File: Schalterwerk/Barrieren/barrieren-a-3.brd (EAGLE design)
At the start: 71.1 x 80 mm, 75 parts, among them Q1 BSS84, Q2 BSS84, Q3 BSS84, Q4 BSS84, Q5 BSS84, Q6 BSS84, X1 PHNX_4P_350CONN_1984989_PXC, X2 PHNX_4P_350CONN_1984989_PXC, X3 PHNX_4P_350CONN_1984989_PXC, X4 PHNX_4P_350CONN_1984989_PXC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

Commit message: Routes the airwires
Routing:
- net GND: track 0.00 -> 173.8 mm, vias 0 -> 6
- net +24V: track 0.00 -> 129.2 mm, vias 0 -> 4
- net +15V: track 0.00 -> 77.0 mm
- net AGND: track 0.00 -> 69.8 mm
- net N$13: track 0.00 -> 51.4 mm
- net +12V: track 0.00 -> 48.5 mm, vias 0 -> 5
- net B3-IS-OP-SCH: track 0.00 -> 43.6 mm, vias 0 -> 1
- net B2-IS-OP-SCH: track 0.00 -> 43.2 mm, vias 0 -> 1
- net B3-IS-CL-SCH: track 0.00 -> 42.2 mm, vias 0 -> 1
- net B2-IS-CL-SCH: track 0.00 -> 42.0 mm, vias 0 -> 1
- net N$20: track 0.00 -> 38.4 mm
- net B3-ACT-CL: track 0.00 -> 36.3 mm
- net N$34: track 0.00 -> 34.7 mm
- net N$31: track 0.00 -> 34.2 mm
- net B2-IS-OP: track 0.00 -> 33.5 mm
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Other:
- board text added: "12V"
- board text added: "24V"

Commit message: removes unneeded mounting hole.
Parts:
- removed H1: MOUNT-HOLE3.3, holes:3,3
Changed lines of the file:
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@@
 <attribute name="NAME" x="57.15" y="30.48" size="1.27" layer="25" font="vector" ratio="10" rot="R180"/>
-</element>
-<element name="H1" library="holes" library_urn="urn:adsk.eagle:library:237" package="3,3" package3d_urn="urn:adsk.eagle:package:14278/1" value="MOUNT-HOLE3.3" x="31.623" y="88.9" smashed="yes" rot="MR0">
-<attribute name="POPULARITY" value="3" x="31.623" y="88.9" size="1.27" layer="28" font="vector" rot="MR0" display="off"/>
 </element>
 <element name="H2" library="holes" library_urn="urn:adsk.eagle:library:237" package="3,3" package3d_urn="urn:adsk.eagle:package:14278/1" value="MOUNT-HOLE3.3" x="4.953" y="5.08" smashed="yes" rot="MR0">

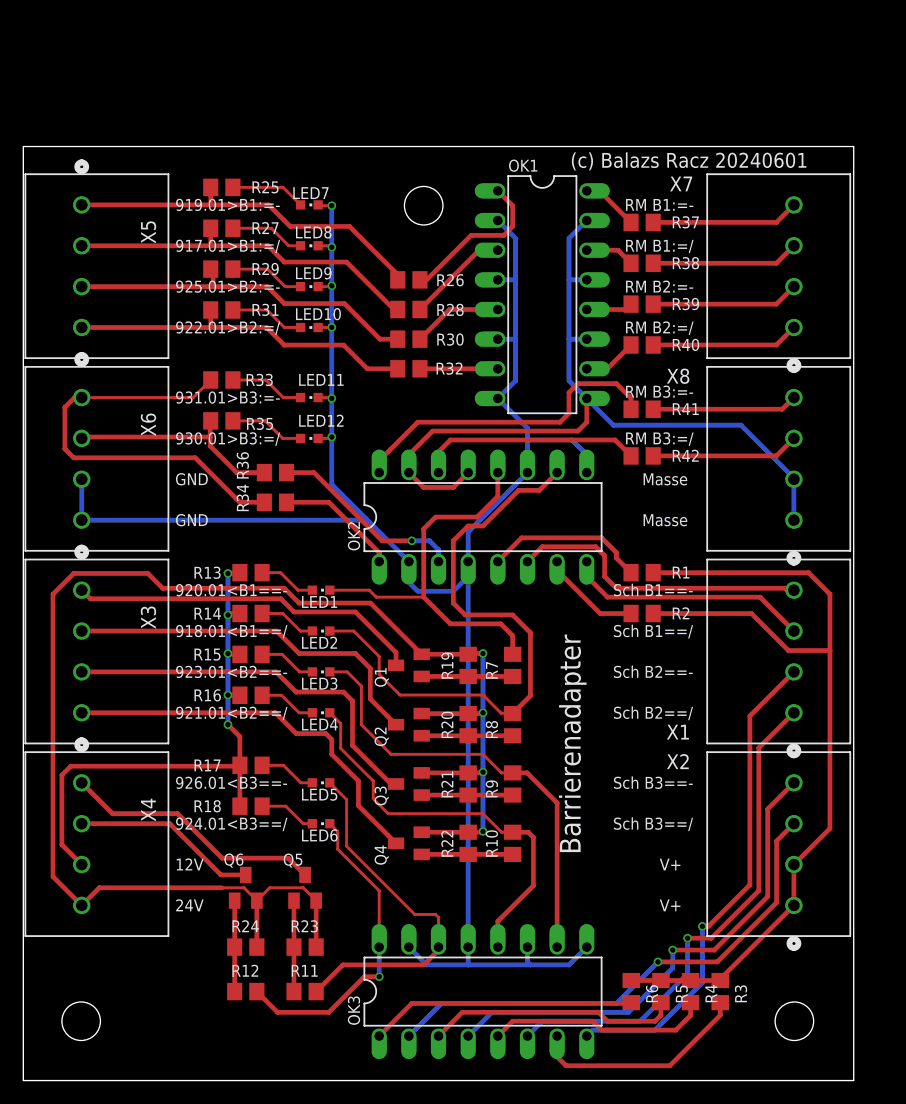
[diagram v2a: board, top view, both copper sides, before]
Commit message: Final tweaks to board. Adds ground planes and vias. Label tweaks.
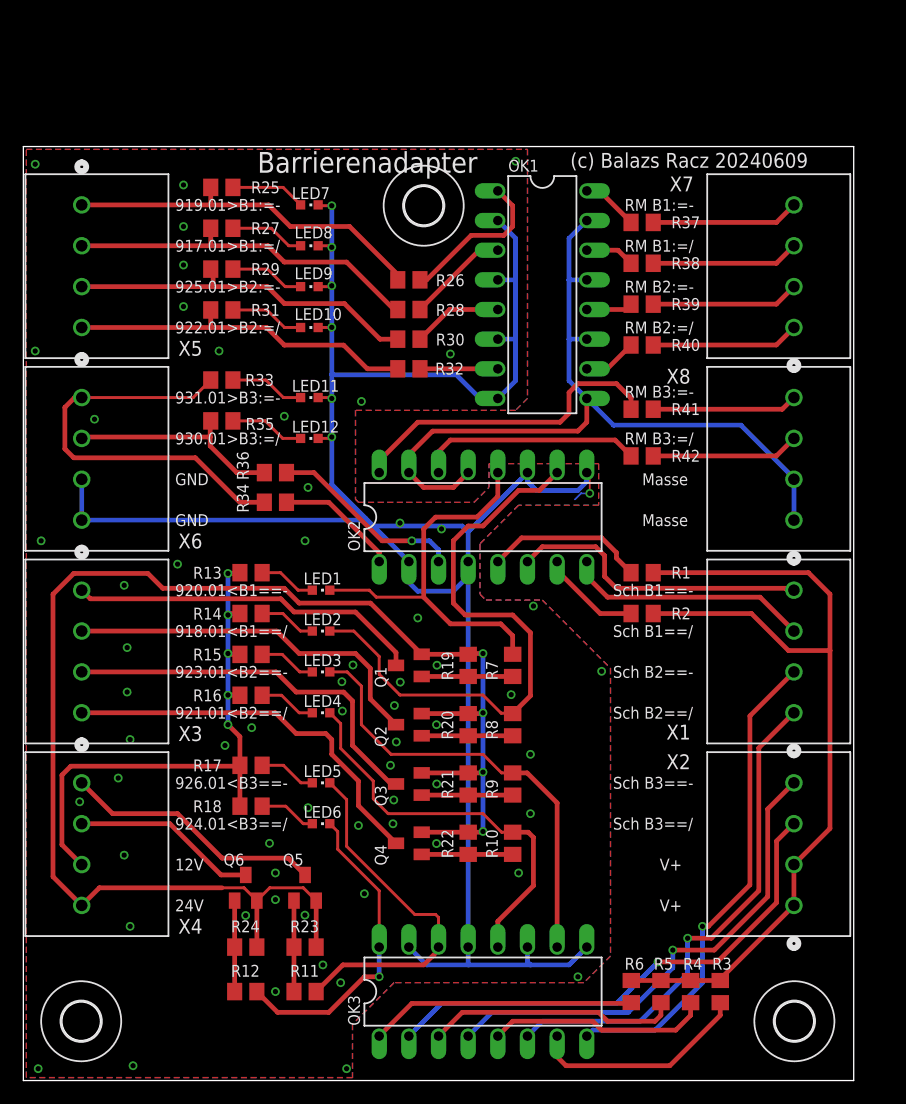
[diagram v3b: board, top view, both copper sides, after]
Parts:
- flipped H2 to the top
- flipped H3 to the top
- flipped H4 to the top
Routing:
- net GND: track 173.8 -> 193.2 mm, vias 6 -> 70
- added copper zone on layer 1, net GND
- added copper zone on layer 16, net GND
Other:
- board text added: "(c) Balazs Racz 20240609"
- board text removed: "(c) Balazs Racz 20240601"
